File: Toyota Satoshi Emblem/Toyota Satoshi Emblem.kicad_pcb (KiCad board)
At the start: 2 copper layers, 175 x 100 mm, 135 parts

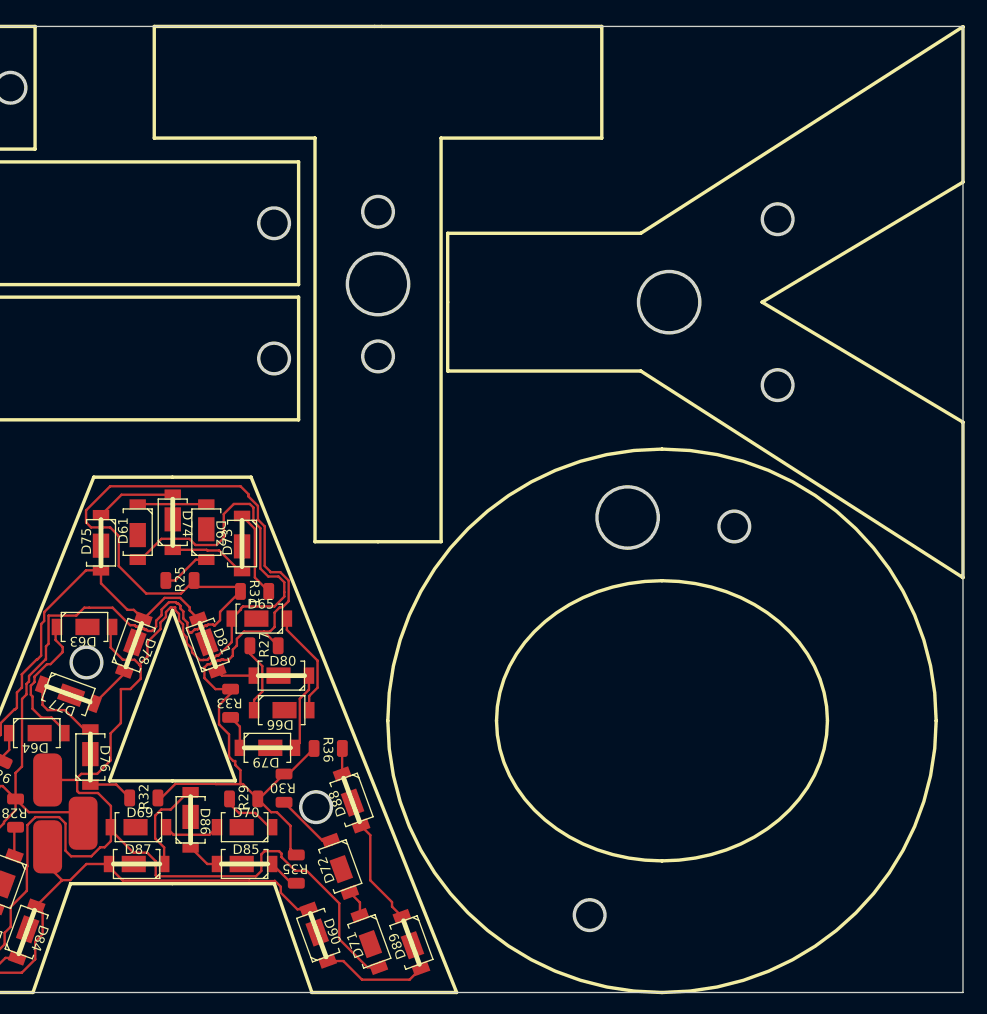
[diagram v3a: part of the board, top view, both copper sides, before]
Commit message: v1.10
Second letter O added
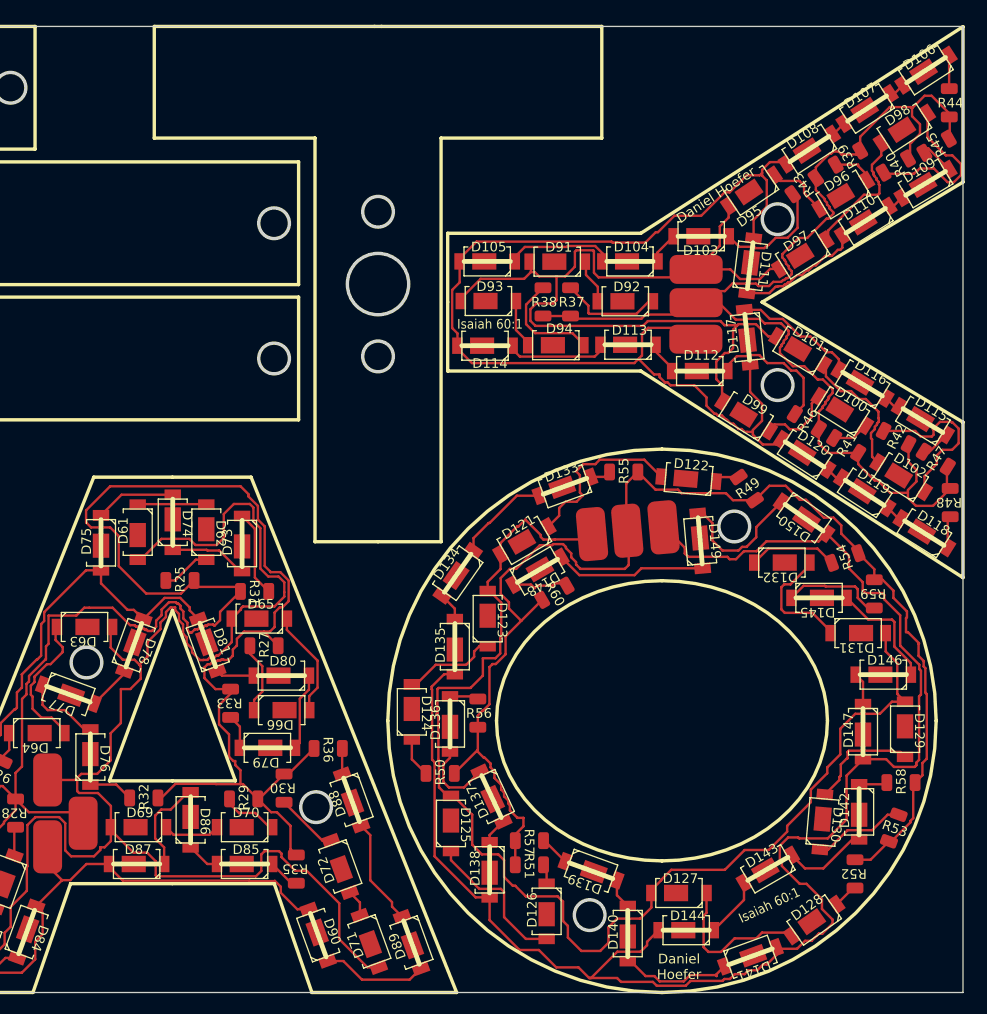
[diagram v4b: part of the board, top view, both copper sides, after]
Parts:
- added D100: WLED, afootprints:5730 LED W, F.Cu at (213.5, 76.8)
- added D101: WLED, afootprints:5730 LED W, F.Cu at (209.2, 70.5)
- added D102: WLED, afootprints:5730 LED W, F.Cu at (219.6, 83.7)
- added D103: ALED, afootprints:5730 LED A, F.Cu at (198.9, 58.7)
- added D104: ALED, afootprints:5730 LED A, F.Cu at (191.5, 61.3)
- added D105: ALED, afootprints:5730 LED A, F.Cu at (176.8, 61.3)
- added D106: ALED, afootprints:5730 LED A, F.Cu at (222.2, 41.5)
- added D107: ALED, afootprints:5730 LED A, F.Cu at (216.1, 45.5)
- added D108: ALED, afootprints:5730 LED A, F.Cu at (210.1, 49.7)
- added D109: ALED, afootprints:5730 LED A, F.Cu at (222.1, 53.2)
- added D110: ALED, afootprints:5730 LED A, F.Cu at (215.9, 57.1)
- added D111: ALED, afootprints:5730 LED A, F.Cu at (204.0, 61.8)
- added D112: ALED, afootprints:5730 LED A, F.Cu at (198.8, 72.7)
- added D113: ALED, afootprints:5730 LED A, F.Cu at (191.3, 70.0)
- added D114: ALED, afootprints:5730 LED A, F.Cu at (176.5, 70.0)
- added D115: ALED, afootprints:5730 LED A, F.Cu at (221.8, 77.8)
- added D116: ALED, afootprints:5730 LED A, F.Cu at (215.6, 74.0)
- added D117: ALED, afootprints:5730 LED A, F.Cu at (203.7, 69.2)
- added D118: ALED, afootprints:5730 LED A, F.Cu at (222.0, 89.5)
- added D119: ALED, afootprints:5730 LED A, F.Cu at (215.8, 85.3)
- added D120: ALED, afootprints:5730 LED A, F.Cu at (209.6, 81.3)
- added D121: WLED, afootprints:5730 LED W, F.Cu at (180.6, 90.2)
- added D122: WLED, afootprints:5730 LED W, F.Cu at (197.6, 83.8)
- added D123: WLED, afootprints:5730 LED W, F.Cu at (176.8, 98.3)
- added D124: WLED, afootprints:5730 LED W, F.Cu at (168.9, 108.0)
- added D125: WLED, afootprints:5730 LED W, F.Cu at (173.0, 119.5)
- added D126: WLED, afootprints:5730 LED W, F.Cu at (182.9, 128.6)
- added D127: WLED, afootprints:5730 LED W, F.Cu at (196.6, 126.7)
- added D128: WLED, afootprints:5730 LED W, F.Cu at (210.6, 129.5)
- added D129: WLED, afootprints:5730 LED W, F.Cu at (220.0, 109.8)
- added D130: WLED, afootprints:5730 LED W, F.Cu at (211.4, 119.3)
- added D131: WLED, afootprints:5730 LED W, F.Cu at (215.2, 99.8)
- added D132: WLED, afootprints:5730 LED W, F.Cu at (207.2, 92.5)
- added D133: ALED, afootprints:5730 LED A, F.Cu at (184.8, 84.6)
- added D134: ALED, afootprints:5730 LED A, F.Cu at (173.7, 93.6)
- added D135: ALED, afootprints:5730 LED A, F.Cu at (173.4, 101.2)
- added D136: ALED, afootprints:5730 LED A, F.Cu at (172.9, 109.2)
- added D137: ALED, afootprints:5730 LED A, F.Cu at (177.2, 116.7)
- added D138: ALED, afootprints:5730 LED A, F.Cu at (177.0, 124.3)
- added D139: ALED, afootprints:5730 LED A, F.Cu at (187.5, 124.4)
- added D140: ALED, afootprints:5730 LED A, F.Cu at (191.3, 130.9)
- added D141: ALED, afootprints:5730 LED A, F.Cu at (204.0, 133.3)
- added D142: ALED, afootprints:5730 LED A, F.Cu at (215.2, 118.3)
- added D143: ALED, afootprints:5730 LED A, F.Cu at (205.8, 124.2)
- added D144: ALED, afootprints:5730 LED A, F.Cu at (197.3, 130.6)
- added D145: ALED, afootprints:5730 LED A, F.Cu at (211.1, 96.2)
- added D146: ALED, afootprints:5730 LED A, F.Cu at (217.8, 104.1)
- added D147: ALED, afootprints:5730 LED A, F.Cu at (215.7, 110.0)
- added D148: ALED, afootprints:5730 LED A, F.Cu at (181.9, 93.3)
- added D149: ALED, afootprints:5730 LED A, F.Cu at (198.8, 90.2)
- added D150: ALED, afootprints:5730 LED A, F.Cu at (209.6, 87.8)
- added D91: WLED, afootprints:5730 LED W, F.Cu at (184.0, 61.4)
- added D92: WLED, afootprints:5730 LED W, F.Cu at (191.1, 65.5)
- added D93: WLED, afootprints:5730 LED W, F.Cu at (176.9, 65.4)
- added D94: WLED, afootprints:5730 LED W, F.Cu at (183.8, 70.0)
- added D95: WLED, afootprints:5730 LED W, F.Cu at (204.1, 54.0)
- added D96: WLED, afootprints:5730 LED W, F.Cu at (213.6, 54.4)
- added D97: WLED, afootprints:5730 LED W, F.Cu at (209.4, 60.6)
- added D98: WLED, afootprints:5730 LED W, F.Cu at (219.9, 47.5)
- added D99: WLED, afootprints:5730 LED W, F.Cu at (203.6, 77.3)
- added R37: 4.7, afootprints:1206 R, F.Cu at (185.4, 65.5)
- added R38: 4.7, afootprints:1206 R, F.Cu at (182.5, 65.5)
- added R39: 4,7, afootprints:1206 R, F.Cu at (214.1, 50.5)
- added R40: 4.7, afootprints:1206 R, F.Cu at (219.1, 51.4)
- added R41: 4.7, afootprints:1206 R, F.Cu at (213.9, 80.4)
- added R42: 4.7, afootprints:1206 R, F.Cu at (219.1, 79.5)
- added R43: 4.7, afootprints:1206 R, F.Cu at (209.6, 53.5)
- added R44: 4.7, afootprints:1206 R, F.Cu at (224.6, 44.9)
- added R45: 4.7, afootprints:1206 R, F.Cu at (223.3, 49.3)
- added R46: 4.7, afootprints:1206 R, F.Cu at (209.9, 77.9)
- added R47: 4.7, afootprints:1206 R, F.Cu at (223.2, 81.8)
- added R48: 4.7, afootprints:1206 R, F.Cu at (224.7, 86.3)
- added R49: 4.7, afootprints:1206 R, F.Cu at (203.7, 84.8)
- added R50: 4.7, afootprints:1206 R, F.Cu at (171.9, 114.3)
- added R51: 4,7, afootprints:1206 R, F.Cu at (181.1, 123.8)
- added R52: 4.7, afootprints:1206 R, F.Cu at (214.8, 124.7)
- added R53: 4.7, afootprints:1206 R, F.Cu at (218.8, 120.0)
- added R54: 4.7, afootprints:1206 R, F.Cu at (213.8, 92.0)
- added R55: 4.7, afootprints:1206 R, F.Cu at (190.9, 83.1)
- added R56: 4.7, afootprints:1206 R, F.Cu at (175.8, 108.1)
- added R57: 4.7, afootprints:1206 R, F.Cu at (181.1, 121.3)
- added R58: 4.7, afootprints:1206 R, F.Cu at (219.6, 115.2)
- added R59: 4.7, afootprints:1206 R, F.Cu at (216.8, 95.7)
- added R60: 4.7, afootprints:1206 R, F.Cu at (183.7, 95.7)
- added REF**: Pad 1, afootprints:Pad 1, F.Cu at (195.0, 88.8)
- added REF**: Pad 1, afootprints:Pad 1, F.Cu at (198.4, 62.1)
- added REF**: Pad 1, afootprints:Pad 1, F.Cu at (198.3, 69.4)
- added REF**: Pad 1, afootprints:Pad 1, F.Cu at (198.4, 65.6)
- added REF**: Pad 1, afootprints:Pad 1, F.Cu at (187.6, 89.5)
- added REF**: Pad 1, afootprints:Pad 1, F.Cu at (191.2, 89.2)
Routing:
- net Net-(D135-Pad1): track 0.00 -> 162.1 mm
- net Net-(R49-Pad1): track 0.00 -> 136.3 mm
- net Net-(D121-Pad1): track 0.00 -> 127.1 mm
- net Net-(J8-Pad2): track 0.00 -> 122.5 mm
- net Net-(D105-Pad1): track 0.00 -> 109.9 mm
- net Net-(D101-Pad1): track 0.00 -> 91.8 mm
- net Net-(D121-Pad2): track 0.00 -> 18.2 mm
- net Net-(D102-Pad2): track 0.00 -> 18.0 mm
- net Net-(D98-Pad2): track 0.00 -> 17.4 mm
- net Net-(D127-Pad2): track 0.00 -> 16.0 mm
- net Net-(D125-Pad2): track 0.00 -> 15.8 mm
- net Net-(D148-Pad1): track 0.00 -> 15.7 mm
- net Net-(D101-Pad2): track 0.00 -> 14.4 mm
- net Net-(D97-Pad2): track 0.00 -> 14.1 mm
- net Net-(D149-Pad1): track 0.00 -> 14.0 mm
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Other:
- outline, holes or cut-outs redrawn

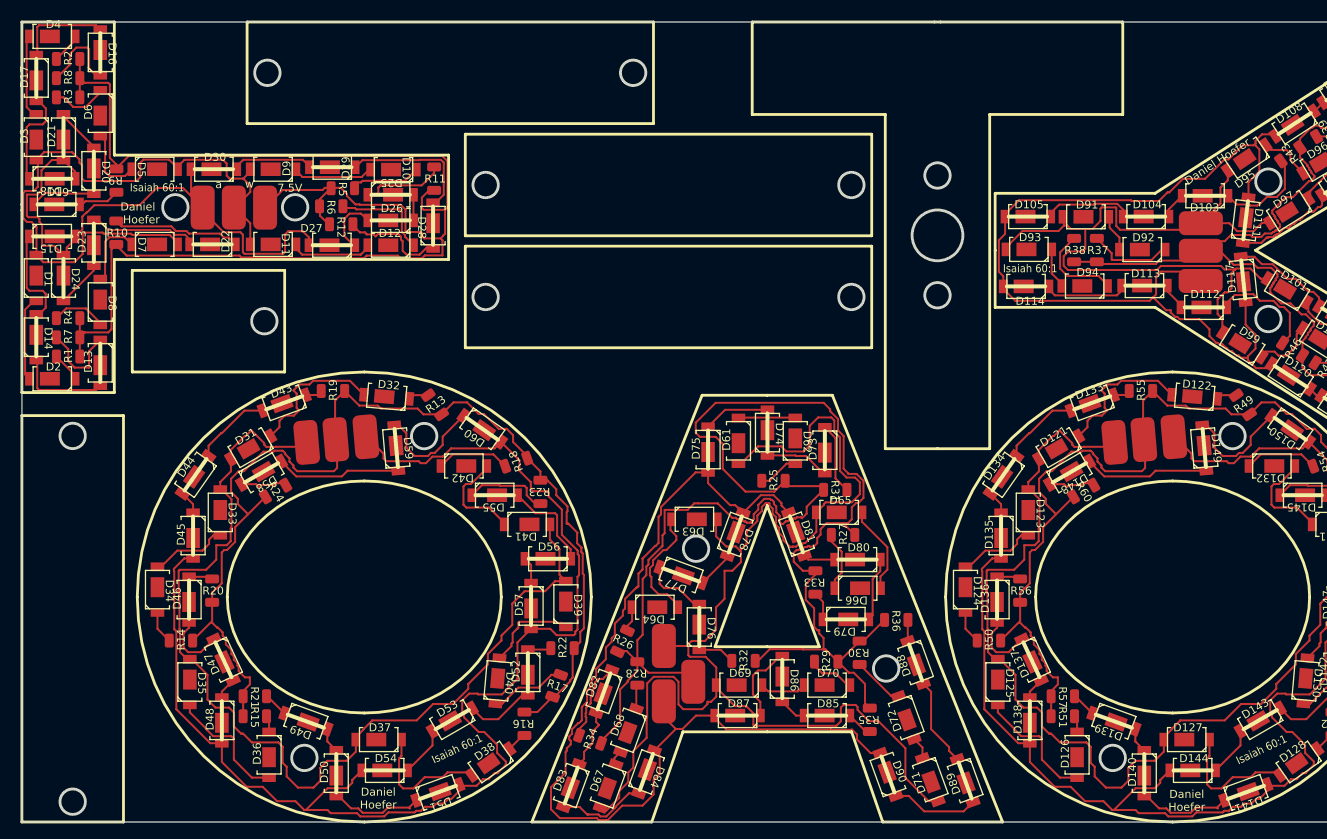
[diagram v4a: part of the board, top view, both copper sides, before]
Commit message: v1.11
All letters and raptor lights are complete. LED board is nearing completion. Photosensor board is remaining.
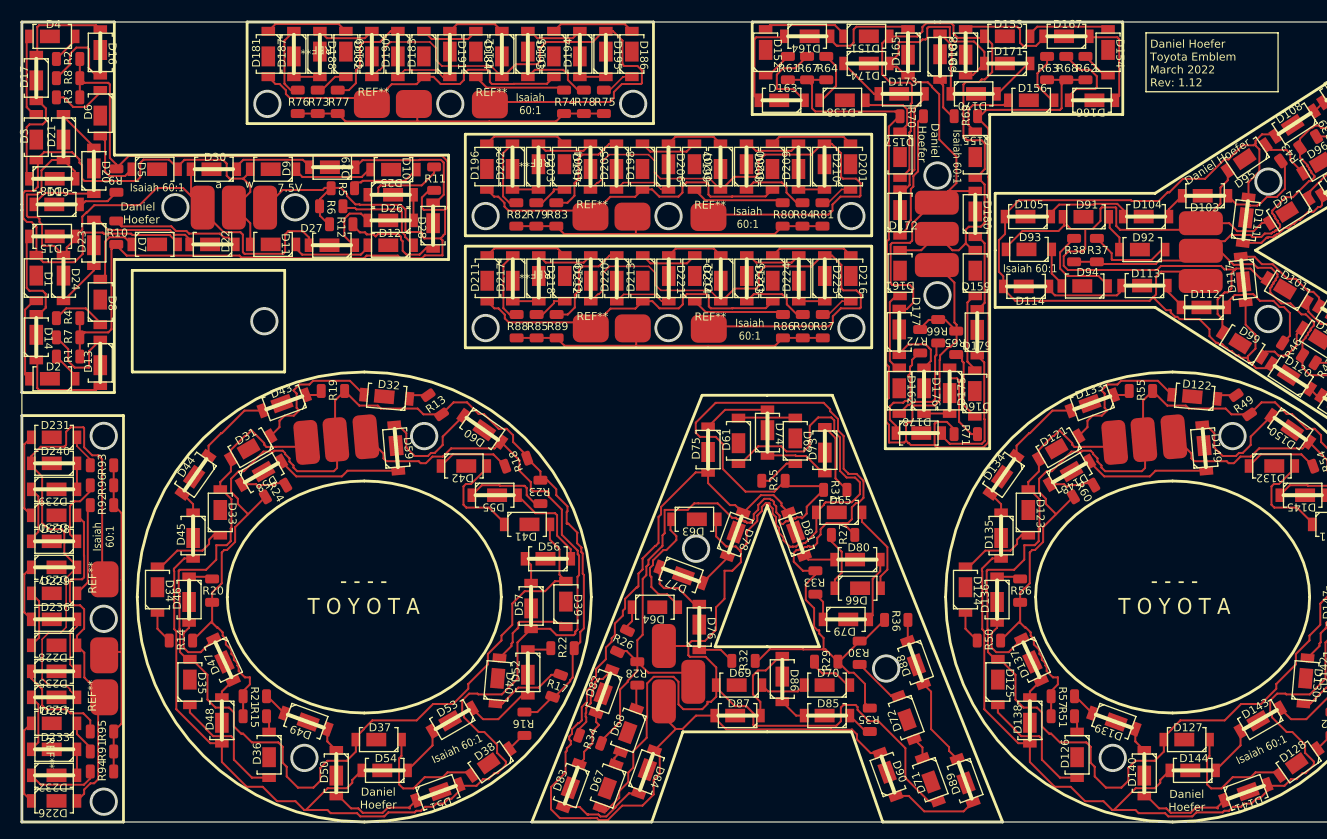
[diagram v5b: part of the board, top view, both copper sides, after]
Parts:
- added D151: WLED, afootprints:5730 LED W, F.Cu at (156.6, 38.8)
- added D152: WLED, afootprints:5730 LED W, F.Cu at (144.0, 40.8)
- added D153: WLED, afootprints:5730 LED W, F.Cu at (174.2, 38.8)
- added D154: WLED, afootprints:5730 LED W, F.Cu at (186.8, 40.8)
- added D155: WLED, afootprints:5730 LED W, F.Cu at (170.2, 53.6)
- added D156: WLED, afootprints:5730 LED W, F.Cu at (177.2, 46.8)
- added D157: WLED, afootprints:5730 LED W, F.Cu at (160.8, 53.6)
- added D158: WLED, afootprints:5730 LED W, F.Cu at (153.6, 46.8)
- added D159: WLED, afootprints:5730 LED W, F.Cu at (170.2, 68.4)
- added D160: WLED, afootprints:5730 LED W, F.Cu at (170.1, 83.4)
- added D161: WLED, afootprints:5730 LED W, F.Cu at (160.8, 68.4)
- added D162: WLED, afootprints:5730 LED W, F.Cu at (160.7, 83.1)
- added D163: ALED, afootprints:5730 LED A, F.Cu at (146.0, 46.8)
- added D164: ALED, afootprints:5730 LED A, F.Cu at (149.2, 38.8)
- added D165: ALED, afootprints:5730 LED A, F.Cu at (161.8, 40.8)
- added D166: ALED, afootprints:5730 LED A, F.Cu at (184.8, 46.8)
- added D167: ALED, afootprints:5730 LED A, F.Cu at (181.6, 38.8)
- added D168: ALED, afootprints:5730 LED A, F.Cu at (169.0, 40.8)
- added D169: ALED, afootprints:5730 LED A, F.Cu at (165.8, 41.3)
- added D170: ALED, afootprints:5730 LED A, F.Cu at (170.0, 46.0)
- added D171: ALED, afootprints:5730 LED A, F.Cu at (174.2, 42.2)
- added D172: ALED, afootprints:5730 LED A, F.Cu at (160.8, 60.8)
- added D173: ALED, afootprints:5730 LED A, F.Cu at (161.0, 46.0)
- added D174: ALED, afootprints:5730 LED A, F.Cu at (156.6, 42.2)
- added D175: ALED, afootprints:5730 LED A, F.Cu at (167.0, 83.1)
- added D176: ALED, afootprints:5730 LED A, F.Cu at (163.8, 83.1)
- added D177: ALED, afootprints:5730 LED A, F.Cu at (160.7, 75.7)
- added D178: ALED, afootprints:5730 LED A, F.Cu at (163.1, 88.4)
- added D179: ALED, afootprints:5730 LED A, F.Cu at (170.4, 75.8)
- added D180: ALED, afootprints:5730 LED A, F.Cu at (170.2, 61.0)
- added D181: WLED, afootprints:5730 LED W, F.Cu at (81.8, 41.0)
- added D182: WLED, afootprints:5730 LED W, F.Cu at (91.5, 41.0)
- added D183: WLED, afootprints:5730 LED W, F.Cu at (101.2, 41.0)
- added D184: WLED, afootprints:5730 LED W, F.Cu at (107.8, 41.0)
- added D185: WLED, afootprints:5730 LED W, F.Cu at (117.5, 41.0)
- added D186: WLED, afootprints:5730 LED W, F.Cu at (127.2, 41.0)
- added D187: ALED, afootprints:5730 LED A, F.Cu at (85.0, 41.0)
- added D188: ALED, afootprints:5730 LED A, F.Cu at (88.2, 41.0)
- added D189: ALED, afootprints:5730 LED A, F.Cu at (94.8, 41.0)
- added D190: ALED, afootprints:5730 LED A, F.Cu at (98.0, 41.0)
- added D191: ALED, afootprints:5730 LED A, F.Cu at (104.5, 41.0)
- added D192: ALED, afootprints:5730 LED A, F.Cu at (111.0, 41.0)
- added D193: ALED, afootprints:5730 LED A, F.Cu at (114.2, 41.0)
- added D194: ALED, afootprints:5730 LED A, F.Cu at (120.8, 41.0)
- added D195: ALED, afootprints:5730 LED A, F.Cu at (124.0, 41.0)
- added D196: WLED, afootprints:5730 LED W, F.Cu at (109.1, 55.1)
- added D197: WLED, afootprints:5730 LED W, F.Cu at (118.8, 55.1)
- added D198: WLED, afootprints:5730 LED W, F.Cu at (128.6, 55.1)
- added D199: WLED, afootprints:5730 LED W, F.Cu at (135.1, 55.1)
- added D200: WLED, afootprints:5730 LED W, F.Cu at (144.8, 55.1)
- added D201: WLED, afootprints:5730 LED W, F.Cu at (154.6, 55.1)
- added D202: ALED, afootprints:5730 LED A, F.Cu at (112.3, 55.1)
- added D203: ALED, afootprints:5730 LED A, F.Cu at (115.6, 55.1)
- added D204: ALED, afootprints:5730 LED A, F.Cu at (122.1, 55.1)
- added D205: ALED, afootprints:5730 LED A, F.Cu at (125.3, 55.1)
- added D206: ALED, afootprints:5730 LED A, F.Cu at (131.8, 55.1)
- added D207: ALED, afootprints:5730 LED A, F.Cu at (138.3, 55.1)
- added D208: ALED, afootprints:5730 LED A, F.Cu at (141.6, 55.1)
- added D209: ALED, afootprints:5730 LED A, F.Cu at (148.1, 55.1)
- added D210: ALED, afootprints:5730 LED A, F.Cu at (151.3, 55.1)
- added D211: WLED, afootprints:5730 LED W, F.Cu at (109.2, 69.0)
- added D212: WLED, afootprints:5730 LED W, F.Cu at (118.9, 69.0)
- added D213: WLED, afootprints:5730 LED W, F.Cu at (128.6, 69.0)
- added D214: WLED, afootprints:5730 LED W, F.Cu at (135.1, 69.0)
- added D215: WLED, afootprints:5730 LED W, F.Cu at (144.9, 69.0)
- added D216: WLED, afootprints:5730 LED W, F.Cu at (154.6, 69.0)
- added D217: ALED, afootprints:5730 LED A, F.Cu at (112.4, 69.0)
- added D218: ALED, afootprints:5730 LED A, F.Cu at (115.6, 69.0)
- added D219: ALED, afootprints:5730 LED A, F.Cu at (122.1, 69.0)
- added D220: ALED, afootprints:5730 LED A, F.Cu at (125.4, 69.0)
- added D221: ALED, afootprints:5730 LED A, F.Cu at (131.9, 69.0)
- added D222: ALED, afootprints:5730 LED A, F.Cu at (138.4, 69.0)
- added D223: ALED, afootprints:5730 LED A, F.Cu at (141.6, 69.0)
- added D224: ALED, afootprints:5730 LED A, F.Cu at (148.1, 69.0)
- added D225: ALED, afootprints:5730 LED A, F.Cu at (151.4, 69.0)
- added D226: WLED, afootprints:5730 LED W, F.Cu at (55.0, 134.4)
- added D227: WLED, afootprints:5730 LED W, F.Cu at (55.0, 124.7)
- added D228: WLED, afootprints:5730 LED W, F.Cu at (55.0, 114.9)
- added D229: WLED, afootprints:5730 LED W, F.Cu at (55.0, 108.4)
- added D230: WLED, afootprints:5730 LED W, F.Cu at (55.0, 98.7)
- added D231: WLED, afootprints:5730 LED W, F.Cu at (55.0, 88.9)
- added D232: ALED, afootprints:5730 LED A, F.Cu at (55.0, 131.2)
- added D233: ALED, afootprints:5730 LED A, F.Cu at (55.0, 127.9)
- added D234: ALED, afootprints:5730 LED A, F.Cu at (55.0, 121.4)
- added D235: ALED, afootprints:5730 LED A, F.Cu at (55.0, 118.2)
- added D236: ALED, afootprints:5730 LED A, F.Cu at (55.0, 111.7)
- added D237: ALED, afootprints:5730 LED A, F.Cu at (55.0, 105.2)
- added D238: ALED, afootprints:5730 LED A, F.Cu at (55.0, 101.9)
- added D239: ALED, afootprints:5730 LED A, F.Cu at (55.0, 95.4)
- added D240: ALED, afootprints:5730 LED A, F.Cu at (55.0, 92.2)
- added R61: 4.7, afootprints:1206 R, F.Cu at (146.8, 42.8)
- added R62: 4.7, afootprints:1206 R, F.Cu at (184.0, 42.8)
- added R63: 4,7, afootprints:1206 R, F.Cu at (179.2, 42.8)
- added R64: 4.7, afootprints:1206 R, F.Cu at (151.6, 42.8)
- added R65: 4.7, afootprints:1206 R, F.Cu at (167.8, 77.1)
- added R66: 4.7, afootprints:1206 R, F.Cu at (165.5, 75.6)
- added R67: 4.7, afootprints:1206 R, F.Cu at (149.2, 42.8)
- added R68: 4.7, afootprints:1206 R, F.Cu at (181.6, 42.8)
- added R69: 4.7, afootprints:1206 R, F.Cu at (169.0, 48.8)
- added R70: 4.7, afootprints:1206 R, F.Cu at (162.2, 48.8)
- added R71: 4.7, afootprints:1206 R, F.Cu at (169.0, 88.5)
- added R72: 4.7, afootprints:1206 R, F.Cu at (163.3, 76.9)
- added R73: 4.7, afootprints:1206 R, F.Cu at (88.0, 47.0)
- added R74: 4.7, afootprints:1206 R, F.Cu at (118.8, 47.0)
- added R75: 4.7, afootprints:1206 R, F.Cu at (123.8, 47.0)
- added R76: 4.7, afootprints:1206 R, F.Cu at (85.5, 47.0)
- added R77: 4.7, afootprints:1206 R, F.Cu at (90.5, 47.0)
- added R78: 4.7, afootprints:1206 R, F.Cu at (121.3, 47.0)
- added R79: 4.7, afootprints:1206 R, F.Cu at (115.3, 61.1)
- added R80: 4.7, afootprints:1206 R, F.Cu at (146.1, 61.1)
- added R81: 4.7, afootprints:1206 R, F.Cu at (151.1, 61.1)
- added R82: 4.7, afootprints:1206 R, F.Cu at (112.8, 61.1)
- added R83: 4.7, afootprints:1206 R, F.Cu at (117.8, 61.1)
- added R84: 4.7, afootprints:1206 R, F.Cu at (148.6, 61.1)
- added R85: 4.7, afootprints:1206 R, F.Cu at (115.4, 75.0)
- added R86: 4.7, afootprints:1206 R, F.Cu at (146.2, 75.0)
- added R87: 4.7, afootprints:1206 R, F.Cu at (151.1, 75.0)
- added R88: 4.7, afootprints:1206 R, F.Cu at (112.9, 75.0)
- added R89: 4.7, afootprints:1206 R, F.Cu at (117.9, 75.0)
- added R90: 4.7, afootprints:1206 R, F.Cu at (148.6, 75.0)
- added R91: 4.7, afootprints:1206 R, F.Cu at (61.0, 128.2)
- added R92: 4.7, afootprints:1206 R, F.Cu at (61.0, 97.4)
- added R93: 4.7, afootprints:1206 R, F.Cu at (61.0, 92.4)
- added R94: 4.7, afootprints:1206 R, F.Cu at (61.0, 130.7)
- added R95: 4.7, afootprints:1206 R, F.Cu at (61.0, 125.7)
- added R96: 4.7, afootprints:1206 R, F.Cu at (61.0, 94.9)
- added REF**: Pad 2, afootprints:Pad 2, F.Cu at (136.8, 61.4)
- added REF**: Pad 2, afootprints:Pad 2, F.Cu at (94.8, 47.2)
- added REF**: Pad 2, afootprints:Pad 2, F.Cu at (61.3, 106.7)
- added REF**: Pad 2, afootprints:Pad 2, F.Cu at (109.5, 47.3)
- added REF**: Pad 2, afootprints:Pad 2, F.Cu at (122.1, 61.3)
- added REF**: Pad 2, afootprints:Pad 2, F.Cu at (122.1, 75.3)
- added REF**: Pad 2, afootprints:Pad 2, F.Cu at (127.4, 75.3)
- added REF**: Pad 2, afootprints:Pad 2, F.Cu at (61.3, 116.2)
- added REF**: Pad 1, afootprints:Pad 1, F.Cu at (165.4, 67.4)
- added REF**: Pad 1, afootprints:Pad 1, F.Cu at (165.4, 59.6)
- added REF**: Pad 2, afootprints:Pad 2, F.Cu at (136.9, 75.3)
- added REF**: Pad 2, afootprints:Pad 2, F.Cu at (61.3, 121.4)
- added REF**: Pad 1, afootprints:Pad 1, F.Cu at (165.4, 63.5)
- added REF**: Pad 2, afootprints:Pad 2, F.Cu at (100.0, 47.2)
- added REF**: Pad 2, afootprints:Pad 2, F.Cu at (127.3, 61.3)
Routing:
- net Net-(R61-Pad1): track 0.00 -> 175.8 mm
- net Net-(D151-Pad1): track 0.00 -> 81.7 mm
- net Net-(D165-Pad1): track 0.00 -> 71.8 mm
- net Net-(D234-Pad1): track 0.00 -> 68.7 mm
- net Net-(D219-Pad1): track 0.00 -> 68.7 mm
- net Net-(D189-Pad1): track 0.00 -> 68.7 mm
- net Net-(D204-Pad1): track 0.00 -> 68.7 mm
- net Net-(D181-Pad1): track 0.00 -> 42.2 mm
- net Net-(D196-Pad1): track 0.00 -> 42.2 mm
- net Net-(D226-Pad1): track 0.00 -> 42.2 mm
- net Net-(D211-Pad1): track 0.00 -> 42.2 mm
- net Net-(R85-Pad1): track 0.00 -> 41.5 mm
- net Net-(R76-Pad1): track 0.00 -> 41.5 mm
- net Net-(R82-Pad1): track 0.00 -> 41.5 mm
- net Net-(R91-Pad1): track 0.00 -> 41.5 mm
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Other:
- outline, holes or cut-outs redrawn
- board text added: "- - - - T O Y O T A"
- board text added: "Daniel Hoefer Toyota Emblem March 2022 Rev: 1.12"
